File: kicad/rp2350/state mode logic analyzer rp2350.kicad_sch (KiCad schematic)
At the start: 142 parts, among them J1 USB0, J2 5V USB0, J3 Exp Out, J4 Exp In, J5 Probe, J6 Probe Power, J7 SWD0, SW1 Reset 0, SW2 Boot 0, U10 74LVC245APW, U11 74LVC245APW, U2 RP2350_80QFN, U3 74HC4520D, U4 LTC6994xS6-1, U5 MCP4725, U6 AD5241BRZ1M, U7 IS25LP128F-JBLE, U9 MCP1826S, Y1 ECS-120-18-33-JEM-TR

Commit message: end of stream commit
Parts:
- removed J3: Exp Out, Connector_PinHeader_2.54mm:PinHeader_2x10_P2.54mm_Horizontal, symbol Connector_Generic:Conn_02x10_Odd_Even
- removed J4: Exp In, Connector_PinSocket_2.54mm:PinSocket_2x10_P2.54mm_Horizontal, symbol Connector_Generic:Conn_02x10_Odd_Even
- J7: STANDARD 01R3466 -> Manufacturer Recommendation
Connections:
- net DN: now also U2.66 (USB_DM)
- net DP: now also U2.67 (USB_DP)
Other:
- note removed: "Extension Connectors"

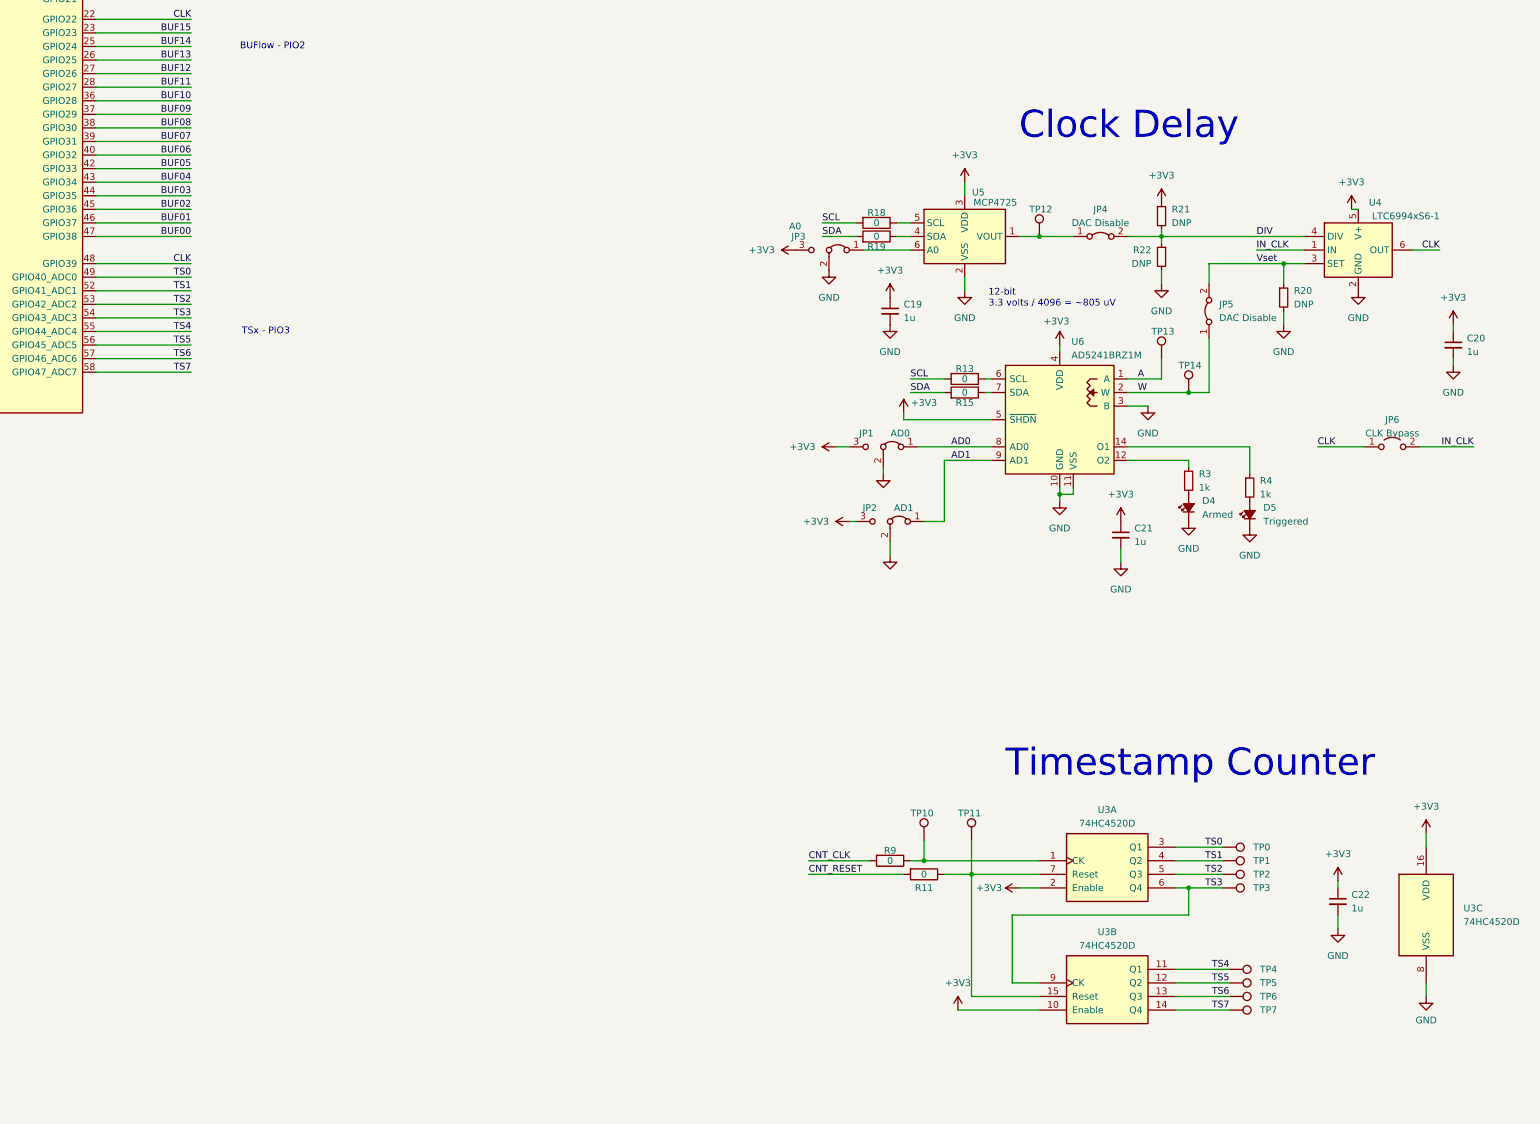
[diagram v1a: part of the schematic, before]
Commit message: removed clock delay and timestamp counter since it can be done in pio.
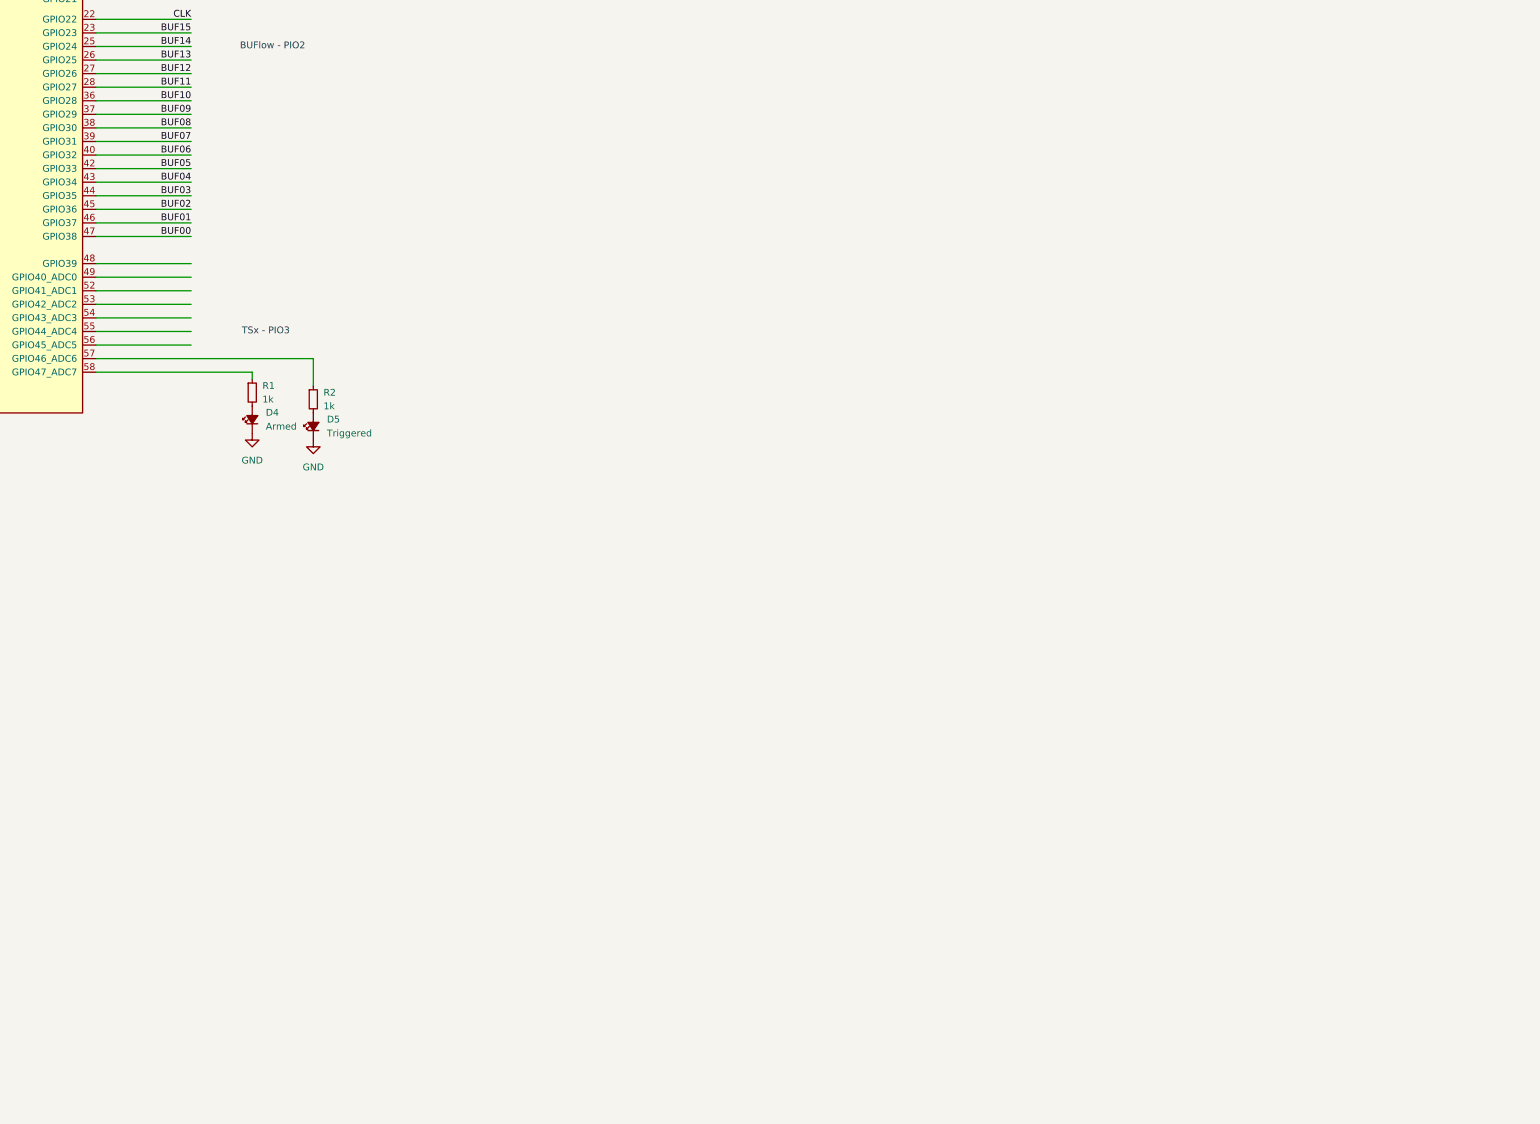
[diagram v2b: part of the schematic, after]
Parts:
- removed C19, C20, C21, C22: 1u, Capacitor_SMD:C_0603_1608Metric_Pad1.08x0.95mm_HandSolder, symbol Device:C_Small
- removed JP1: AD0, Jumper:SolderJumper-3_P1.3mm_Bridged2Bar12_Pad1.0x1.5mm, symbol Jumper:Jumper_3_Bridged12
- removed JP2: AD1, Jumper:SolderJumper-3_P1.3mm_Bridged2Bar12_Pad1.0x1.5mm, symbol Jumper:Jumper_3_Bridged12
- removed JP3: A0, Jumper:SolderJumper-3_P1.3mm_Bridged2Bar12_Pad1.0x1.5mm, symbol Jumper:Jumper_3_Bridged12
- removed JP4, JP5: DAC Disable, Jumper:SolderJumper-2_P1.3mm_Bridged2Bar_Pad1.0x1.5mm, symbol Jumper:Jumper_2_Bridged
- removed JP6: CLK Bypass, Jumper:SolderJumper-2_P1.3mm_Open_Pad1.0x1.5mm, symbol Jumper:Jumper_2_Open
- removed R11, R13, R15, R18, R19, R9: 0, Resistor_SMD:R_0603_1608Metric_Pad0.98x0.95mm_HandSolder, symbol Device:R
- removed R20, R21, R22: DNP, Resistor_SMD:R_0603_1608Metric_Pad0.98x0.95mm_HandSolder, symbol Device:R_Small
- removed R3, R4: 1k, Resistor_SMD:R_0603_1608Metric_Pad0.98x0.95mm_HandSolder, symbol Device:R_Small
- removed TP0, TP1, TP10, TP11, TP12, TP13, TP14, TP2, TP3, TP4, TP5, TP6, TP7: TestPoint_Harwin, My Libraries:Harwin-S1751-46-Test-Point, symbol My Library:TestPoint_Harwin
- removed U3: 74HC4520D, Package_SO:TSSOP-16_4.4x5mm_P0.65mm, symbol 4xxx:4520
- removed U4: LTC6994xS6-1, Package_TO_SOT_SMD:TSOT-23-6, symbol Timer:LTC6994xS6-1
- removed U5: MCP4725, Package_TO_SOT_SMD:SOT-23-6, symbol Analog_DAC:MCP4725xxx-xCH
- removed U6: AD5241BRZ1M, Package_SO:SOIC-16_3.9x9.9mm_P1.27mm, symbol My Library:AD5241
- added R1, R2: 1k, Resistor_SMD:R_0603_1608Metric_Pad0.98x0.95mm_HandSolder, symbol Device:R_Small
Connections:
- net CLK: no longer U2.48 (GPIO39)
- net at D4.2 (A): now also R1.2
- net at D5.2 (A): now also R2.2
- net TS0: no longer names the net of U2.49 (GPIO40_ADC0)
- net TS1: no longer names the net of U2.52 (GPIO41_ADC1)
- net TS2: no longer names the net of U2.53 (GPIO42_ADC2)
- net TS3: no longer names the net of U2.54 (GPIO43_ADC3)
- net TS4: no longer names the net of U2.55 (GPIO44_ADC4)
- net TS5: no longer names the net of U2.56 (GPIO45_ADC5)
- net TS6: no longer names the net of U2.57 (GPIO46_ADC6)
- net TS6: now also R2.1
- net TS7: no longer names the net of U2.58 (GPIO47_ADC7)
- net TS7: now also R1.1
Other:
- note removed: "12-bit 3.3 volts / 4096 = ~805 uV"
- note removed: "Clock Delay"
- note removed: "Timestamp Counter"

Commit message: moved to 2-supply buffer design
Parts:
- removed U10, U11: 74LVC245APW, Package_SO:TSSOP-20_4.4x6.5mm_P0.65mm, symbol 74xx:74HC245
- added C10, C11, C7, C8, C9: 1u, Capacitor_SMD:C_0603_1608Metric_Pad1.08x0.95mm_HandSolder, symbol Device:C_Small
- added J3: Probe_Hi, Connector_PinHeader_2.54mm:PinHeader_2x13_P2.54mm_Vertical, symbol Connector_Generic:Conn_02x13_Odd_Even
- added J4: Probe Power, Connector_PinHeader_2.54mm:PinHeader_1x03_P2.54mm_Vertical, symbol Connector_Generic:Conn_01x03
- added R49, R50, R51, R52, R53, R54, R55, R56, R57, R58, R59, R60, R61, R62, R63, R64, R73, R74: 220, Resistor_SMD:R_0603_1608Metric, symbol Device:R_Small
- added TP116, TP117, TP118, TP119, TP120, TP121, TP122, TP123, TP124, TP125, TP126, TP127, TP128, TP129, TP130, TP131, TP132, TP133: TestPoint_Harwin, My Libraries:Harwin-S1751-46-Test-Point, symbol My Library:TestPoint_Harwin
- added U12, U4, U5, U6: SN74LVC8T245, Package_SO:SSOP-24_3.9x8.7mm_P0.635mm, symbol Logic_LevelTranslator:SN74LVC8T245
- added U13: SN74LVC2T45DCUR, Package_SO:SSOP-8_2.95x2.8mm_P0.65mm, symbol Logic_LevelTranslator:SN74LVC2T45DCUR
- J5: value Probe -> Probe_Lo; footprint Connector_PinHeader_2.54mm:PinHeader_2x12_P2.54mm_Vertical -> Connector_PinHeader_2.54mm:PinHeader_2x13_P2.54mm_Vertical; symbol Connector_Generic:Conn_02x12_Odd_Even -> Connector_Generic:Conn_02x13_Odd_Even
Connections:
- net A0 is gone; now on net IN00: R25.2
- net A1 is gone; now on net IN01: R26.2
- net A10 is gone; now on net IN13: R35.2
- net A11 is gone; now on net IN12: R36.2
- net A12 is gone; now on net IN11: R37.2
- net A13 is gone; now on net IN10: R38.2
- net A14 is gone; now on net IN09: R39.2
- net A15 is gone; now on net IN08: R40.2
- net A2 is gone; now on net IN02: R27.2
- net A3 is gone; now on net IN03: R28.2
- net A4 is gone; now on net IN04: R29.2
- net A5 is gone; now on net IN05: R30.2
- net A6 is gone; now on net IN06: R31.2
- net A7 is gone; now on net IN07: R32.2
- net A8 is gone; now on net IN15: R33.2
- net A9 is gone; now on net IN14: R34.2
- net CNT_CLK is gone; now on net BUF31: U2.79 (GPIO2)
- net LA_Enable is gone; now on net BUF29: U2.1 (GPIO4)
- net +3V3: now also C11.1, C7.1, C8.1, C9.1, J4.3 (Pin_3), U12.1 (V_{CCA}), U12.23 (V_{CCB}), U12.24 (V_{CCB}), U13.1 (VCCA), U13.8 (VCCB), U4.1 (V_{CCA}), U4.23 (V_{CCB}), U4.24 (V_{CCB}), U5.1 (V_{CCA}), U5.23 (V_{CCB}), U5.24 (V_{CCB}), U6.1 (V_{CCA}), U6.23 (V_{CCB}), U6.24 (V_{CCB})
- net +5V: now also C10.1, J4.1 (Pin_1)
- net BUF00: now also U2.44 (GPIO35), U12.10 (A8); no longer U2.47 (GPIO38)
- net BUF01: now also U2.43 (GPIO34), U12.9 (A7); no longer U2.46 (GPIO37)
- net BUF02: now also U2.42 (GPIO33), U12.8 (A6); no longer U2.45 (GPIO36)
- net BUF03: now also U2.40 (GPIO32), U12.7 (A5); no longer U2.44 (GPIO35)
- net BUF04: now also U2.39 (GPIO31), U12.6 (A4); no longer U2.43 (GPIO34)
- net BUF05: now also U2.38 (GPIO30), U12.5 (A3); no longer U2.42 (GPIO33)
- net BUF06: now also U2.37 (GPIO29), U12.4 (A2); no longer U2.40 (GPIO32)
- net BUF07: now also U2.36 (GPIO28), U12.3 (A1); no longer U2.39 (GPIO31)
- net BUF08: now also U2.28 (GPIO27), U4.10 (A8); no longer U2.38 (GPIO30)
- net BUF09: now also U2.27 (GPIO26), U4.9 (A7); no longer U2.37 (GPIO29)
- net BUF10: now also U2.26 (GPIO25), U4.8 (A6); no longer U2.36 (GPIO28)
- net BUF11: now also U2.25 (GPIO24), U4.7 (A5); no longer U2.28 (GPIO27)
- net BUF12: now also U2.23 (GPIO23), U4.6 (A4); no longer U2.27 (GPIO26)
- net BUF13: now also U2.22 (GPIO22), U4.5 (A3); no longer U2.26 (GPIO25)
- net BUF14: now also U2.21 (GPIO21), U4.4 (A2); no longer U2.25 (GPIO24)
- net BUF15: now also U2.20 (GPIO20), U4.3 (A1); no longer U2.23 (GPIO23)
- net BUF16: now also U2.17 (GPIO17), TP116.1, U5.10 (A8); no longer U2.21 (GPIO21)
- net BUF17: now also U2.16 (GPIO16), TP117.1, U5.9 (A7); no longer U2.20 (GPIO20)
- net BUF18: now also U2.14 (GPIO15), TP118.1, U5.8 (A6); no longer U2.19 (GPIO19)
- net BUF19: now also U2.13 (GPIO14), TP119.1, U5.7 (A5); no longer U2.18 (GPIO18)
- net BUF20: now also U2.12 (GPIO13), TP120.1, U5.6 (A4); no longer U2.17 (GPIO17)
- net BUF21: now also U2.11 (GPIO12), TP121.1, U5.5 (A3); no longer U2.16 (GPIO16)
- net BUF22: now also U2.9 (GPIO11), TP122.1, U5.4 (A2); no longer U2.14 (GPIO15)
- net BUF23: now also U2.8 (GPIO10), TP123.1, U5.3 (A1); no longer U2.13 (GPIO14)
- net BUF24: now also U2.7 (GPIO9), TP124.1, U6.10 (A8); no longer U2.12 (GPIO13)
- net BUF25: now also U2.6 (GPIO8), TP125.1, U6.9 (A7); no longer U2.11 (GPIO12)
- net BUF26: now also U2.4 (GPIO7), TP126.1, U6.8 (A6); no longer U2.9 (GPIO11)
- net BUF27: now also U2.3 (GPIO6), TP127.1, U6.7 (A5); no longer U2.8 (GPIO10)
- net BUF28: now also U2.2 (GPIO5), TP128.1, U6.6 (A4); no longer U2.7 (GPIO9)
- net BUF29: now also TP129.1, U6.5 (A3); no longer U2.6 (GPIO8)
- net BUF30: now also U2.80 (GPIO3), TP130.1, U6.4 (A2); no longer U2.4 (GPIO7)
- net BUF31: now also TP131.1, U6.3 (A1); no longer U2.3 (GPIO6)
- net CLK: now also U2.19 (GPIO19), U2.78 (GPIO1), TP132.1, U13.3 (A2); no longer U2.2 (GPIO5), U2.22 (GPIO22)
- net GND: now also J5.10 (Pin_10), J5.15 (Pin_15), J5.16 (Pin_16), J5.21 (Pin_21), J5.22 (Pin_22), J5.3 (Pin_3), J5.4 (Pin_4), J5.9 (Pin_9), C10.2, C11.2, C7.2, C8.2, C9.2, J3.10 (Pin_10), J3.15 (Pin_15), J3.16 (Pin_16), J3.21 (Pin_21), J3.22 (Pin_22), J3.3 (Pin_3), J3.4 (Pin_4), J3.9 (Pin_9), J4.2 (Pin_2), U12.11 (GND), U12.12 (GND), U12.13 (GND), U13.4 (GND), U4.11 (GND), U4.12 (GND), U4.13 (GND), U5.11 (GND), U5.12 (GND), U5.13 (GND), U6.11 (GND), U6.12 (GND), U6.13 (GND); no longer J5.1 (Pin_1), J5.13 (Pin_13), J5.14 (Pin_14), J5.19 (Pin_19), J5.20 (Pin_20), J5.7 (Pin_7), J5.8 (Pin_8)
- net IN00: now also J5.6 (Pin_6); no longer J5.4 (Pin_4), R25.1
- net IN01: now also J5.5 (Pin_5); no longer J5.3 (Pin_3), R26.1
- net IN02: now also J5.8 (Pin_8); no longer J5.6 (Pin_6), R27.1
- net IN03: now also J5.7 (Pin_7); no longer J5.5 (Pin_5), R28.1
- net IN04: now also J5.12 (Pin_12); no longer J5.10 (Pin_10), R29.1
- net IN05: now also J5.11 (Pin_11); no longer J5.9 (Pin_9), R30.1
- net IN06: now also J5.14 (Pin_14); no longer J5.12 (Pin_12), R31.1
- net IN07: now also J5.13 (Pin_13); no longer J5.11 (Pin_11), R32.1
- net IN08: now also J5.18 (Pin_18); no longer J5.16 (Pin_16), R33.1
- net IN09: now also J5.17 (Pin_17); no longer J5.15 (Pin_15), R34.1
- net IN10: now also J5.20 (Pin_20); no longer J5.18 (Pin_18), R35.1
- net IN11: now also J5.19 (Pin_19); no longer J5.17 (Pin_17), R36.1
- net IN12: now also J5.24 (Pin_24); no longer J5.22 (Pin_22), R37.1
- net IN13: now also J5.23 (Pin_23); no longer J5.21 (Pin_21), R38.1
- net IN14: now also J5.26 (Pin_26); no longer J5.24 (Pin_24), R39.1
- net IN15: now also J5.25 (Pin_25); no longer J5.23 (Pin_23), R40.1
- net SCL: now also U2.53 (GPIO42_ADC2); no longer U2.78 (GPIO1)
- net SDA: now also U2.52 (GPIO41_ADC1); no longer U2.77 (GPIO0)
- net at U2.55 (GPIO44_ADC4): now also R43.1
- removed net CNT_RESET: R43.1, U2.80 (GPIO3)
- net IN_CLK renamed INCLK
- net INCLK: now also J3.2 (Pin_2), R74.2
- new net B0: R25.1, U12.14 (B8)
- new net B1: R26.1, U12.15 (B7)
- new net B10: R38.1, U4.16 (B6)
- new net B11: R37.1, U4.17 (B5)
- new net B12: R36.1, U4.18 (B4)
- new net B13: R35.1, U4.19 (B3)
- new net B14: R34.1, U4.20 (B2)
- new net B15: R33.1, U4.21 (B1)
- new net B16: R56.1, U5.14 (B8)
- new net B17: R55.1, U5.15 (B7)
- new net B18: R54.1, U5.16 (B6)
- new net B19: R53.1, U5.17 (B5)
- new net B2: R27.1, U12.16 (B6)
- new net B20: R52.1, U5.18 (B4)
- new net B21: R51.1, U5.19 (B3)
- new net B22: R50.1, U5.20 (B2)
- new net B23: R49.1, U5.21 (B1)
- new net B24: R64.1, U6.14 (B8)
- new net B25: R63.1, U6.15 (B7)
- new net B26: R62.1, U6.16 (B6)
- new net B27: R61.1, U6.17 (B5)
- new net B28: R60.1, U6.18 (B4)
- new net B29: R59.1, U6.19 (B3)
- new net B3: R28.1, U12.17 (B5)
- new net B30: R58.1, U6.20 (B2)
- new net B31: R57.1, U6.21 (B1)
- new net B32: R74.1, U13.6 (B2)
- new net B33: R73.1, U13.7 (B1)
- new net B4: R29.1, U12.18 (B4)
- new net B5: R30.1, U12.19 (B3)
- new net B6: R31.1, U12.20 (B2)
- new net B7: R32.1, U12.21 (B1)
- new net B8: R40.1, U4.14 (B8)
- new net B9: R39.1, U4.15 (B7)
- new net IN16: J3.6 (Pin_6), R56.2
- new net IN17: J3.5 (Pin_5), R55.2
- new net IN18: J3.8 (Pin_8), R54.2
- new net IN19: J3.7 (Pin_7), R53.2
- new net IN20: J3.12 (Pin_12), R52.2
- new net IN21: J3.11 (Pin_11), R51.2
- new net IN22: J3.14 (Pin_14), R50.2
- new net IN23: J3.13 (Pin_13), R49.2
- new net IN24: J3.18 (Pin_18), R64.2
- new net IN25: J3.17 (Pin_17), R63.2
- new net IN26: J3.20 (Pin_20), R62.2
- new net IN27: J3.19 (Pin_19), R61.2
- new net IN28: J3.24 (Pin_24), R60.2
- new net IN29: J3.23 (Pin_23), R59.2
- new net IN30: J3.26 (Pin_26), R58.2
- new net IN31: J3.25 (Pin_25), R57.2
- new net INQUAL: J3.1 (Pin_1), J5.1 (Pin_1), R73.2
- new net QUAL: TP133.1, U13.2 (A1), U2.18 (GPIO18), U2.77 (GPIO0)
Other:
- note added: "MCU (RP2354b)"
- note added: "TODO: - Switch to Stamp XL - Add LDO with DigiPot - Add OLED Header? - More decoupling for the BUS XCVRs"
- note removed: "BUFhigh - PIO1"
- note removed: "BUFlow - PIO2"
- note removed: "MCU (RP2350b)"
- moved on the sheet: C1, C13, C14, C15, C16, C17, C18, C2, C23, C24, C25, C26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

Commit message: rough layout check going to re do it for real
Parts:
- added U1: NCP1117-ADJ_SOT223, Package_TO_SOT_SMD:SOT-223-3_TabPin2, symbol Regulator_Linear:NCP1117-ADJ_SOT223
- added U3: AD5241BRZ1M, Package_SO:SOIC-14_3.9x8.7mm_P1.27mm, symbol My Library:AD5241
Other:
- note added: "4 ch esd diode: SRDA05-4BTG"
- note added: "TODO: - Switch to Stamp XL - Add LDO with DigiPot - Add OLED Header? - More decoupling for the BUS XCVRs - add ESD protection to inputs"
- note removed: "TODO: - Switch to Stamp XL - Add LDO with DigiPot - Add OLED Header? - More decoupling for the BUS XCVRs"
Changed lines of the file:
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@@
 		)
 	)
-	(text "TODO:\n- Switch to Stamp XL\n- Add LDO with DigiPot\n- Add OLED Header?\n- More decoupling for the BUS XCVRs\n\n"
+	(text "TODO:\n- Switch to Stamp XL\n- Add LDO with DigiPot\n- Add OLED Header?\n- More decoupling for the BUS XCVRs\n- add ESD protection to inputs\n"
 		(exclude_from_sim no)
 		(at 514.35 32.385 0)
@@
 		)
 	)
+	(text "4 ch esd diode: SRDA05-4BTG"
+		(exclude_from_sim no)
+		(at 175.26 339.725 0)
+		(effects
+			(font
+				(size 1.27 1.27)
+			)
+		)
+	)
 	(text "Probe Inputs"
 		(exclude_from_sim no)
@@
 	)
 	(symbol
+		(lib_id "My Library:AD5241")
+		(at 374.65 360.68 0)
+		(unit 1)
+		(exclude_from_sim no)
+		(in_bom yes)
+		(on_board yes)
+		(dnp no)
+		(fields_autoplaced yes)
+		(property "Reference" "U3"
+			(at 376.8441 346.075 0)
+			(effects
+				(font
+					(size 1.27 1.27)
+				)
+				(justify left)
+			)
+		)
+		(property "Value" "AD5241BRZ1M"
+			(at 376.8441 348.615 0)
+			(effects
+				(font
+					(size 1.27 1.27)
+				)
+				(justify left)
+			)
+		)
+		(property "Footprint" "Package_SO:SOIC-14_3.9x8.7mm_P1.27mm"
+			(at 374.65 375.92 0)
+			(effects
+				(font
+					(size 1.27 1.27)
+				)
+				(hide yes)
+			)
+		)
+		(property "Datasheet" "https://www.analog.com/media/en/technical-documentation/data-sheets/ad5241_5242.pdf"
+			(at 377.19 365.76 0)
+			(effects
+				(font
+					(size 1.27 1.27)
+				)
+				(hide yes)
+			)
+		)
+		(property "Description" ""
+			(at 374.65 360.68 0)
+			(effects
+				(font
+					(size 1.27 1.27)
+				)
+				(hide yes)
+			)
+		)
+		(property "SPN" "49AK9193"
+			(at 374.65 360.68 0)
+			(effects
+				(font
+					(size 1.27 1.27)
+				)
+				(hide yes)
+			)
+		)
+		(pin "1"
+		)
+		(pin "10"
+		)
+		(pin "11"
+		)
+		(pin "12"
+		)
+		(pin "13"
+		)
+		(pin "14"
+		)
+		(pin "2"
+		)
+		(pin "3"
+		)
+		(pin "4"
+		)
+		(pin "5"
+		)
+		(pin "6"
+		)
+		(pin "7"
+		)
+		(pin "8"
+		)
+		(pin "9"
+		)
+		(instances
+			(project "state mode logic analyzer rp2350"
+				(path "/7975ca51-68cd-4bb7-8d39-236fa03ee415"
+					(reference "U3")
+					(unit 1)
+				)
+			)
+		)
+	)
+	(symbol
 		(lib_id "Device:R_Small")
 		(at 93.98 334.01 270)
@@
 					(unit 1)
 				)
+			)
+		)
+	)
+	(symbol
+		(lib_id "Regulator_Linear:NCP1117-ADJ_SOT223")
+		(at 332.74 355.6 0)
+		(unit 1)
+		(exclude_from_sim no)
+		(in_bom yes)
+		(on_board yes)
+		(dnp no)
+		(fields_autoplaced yes)
+		(property "Reference" "U1"
+			(at 332.74 349.25 0)
+			(effects
+				(font
+					(size 1.27 1.27)
+				)
+			)
+		)
+		(property "Value" "NCP1117-ADJ_SOT223"
+			(at 332.74 351.79 0)
+			(effects
+				(font
+					(size 1.27 1.27)
+				)
+			)
+		)
+		(property "Footprint" "Package_TO_SOT_SMD:SOT-223-3_TabPin2"
+			(at 332.74 350.52 0)
+			(effects
+				(font
+					(size 1.27 1.27)
+				)
+				(hide yes)
+			)
+		)
+		(property "Datasheet" "http://www.onsemi.com/pub_link/Collateral/NCP1117-D.PDF"
+			(at 335.28 361.95 0)
+			(effects
+				(font
+					(size 1.27 1.27)
+				)
+				(hide yes)
+			)
+		)
+		(property "Description" "1A Low drop-out regulator, Adjustable Output 1.25 - 18.8V, SOT-223"
+			(at 332.74 355.6 0)
+			(effects
+				(font
+					(size 1.27 1.27)
+				)
+				(hide yes)
+			)
+		)
+		(property "MPN" "NCP1117LPSTADT3G "
+			(at 332.74 355.6 0)
+			(effects
+				(font
+					(size 1.27 1.27)
+				)
+				(hide yes)
+			)
+		)
+		(pin "3"
+		)
+		(pin "2"
+		)
+		(pin "1"
+		)
+		(instances
+			(project ""
+				(path "/7975ca51-68cd-4bb7-8d39-236fa03ee415"
+					(reference "U1")
+					(unit 1)
+				)
